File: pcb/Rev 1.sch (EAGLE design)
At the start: 216 parts, among them J1 3220-10-0100-00, J2 10118194-0001LF, J3 B2B-PH-K-S(LF)(SN), Q1 MMBT3904,215MMBT3904,215, Q12 MMBT3904,215MMBT3904,215, Q13 MMBT3904,215MMBT3904,215, Q14 MMBT3904,215MMBT3904,215, Q15 MMBT3904,215MMBT3904,215, Q16 TEFT4300, Q17 TEFT4300, Q18 TEFT4300, Q19 TEFT4300, Q20 MMBT3904,215MMBT3904,215, Q21 MMBT3904,215MMBT3904,215, Q22 MMBT3904,215MMBT3904,215, Q23 MMBT3904,215MMBT3904,215, Q24 TEFT4300, Q25 TEFT4300, Q26 TEFT4300, Q27 TEFT4300, Q28 SI7157DP, Q29 SI7157DP, Q30 MMBT3906, Q31 MMBT3906, Q32 SI7157DP, Q33 MMBT3906, Q34 MMBT3906, U1 ATSAMD21G18A-MU, U10 DRV8871, U11 PCAL6416A, U12 MAX7315, U2 AP3441, U3 TPS61089, U4 BNO055, U5 MCP73811, U7 DRV8871, U8 DRV8871, U9 DRV8871

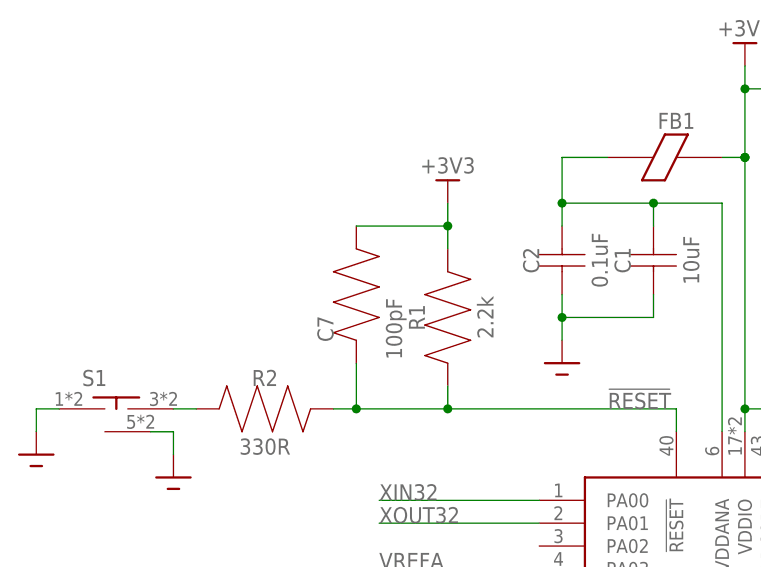
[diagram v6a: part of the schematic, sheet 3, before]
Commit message: Fixed C7 that was somehow a resistor
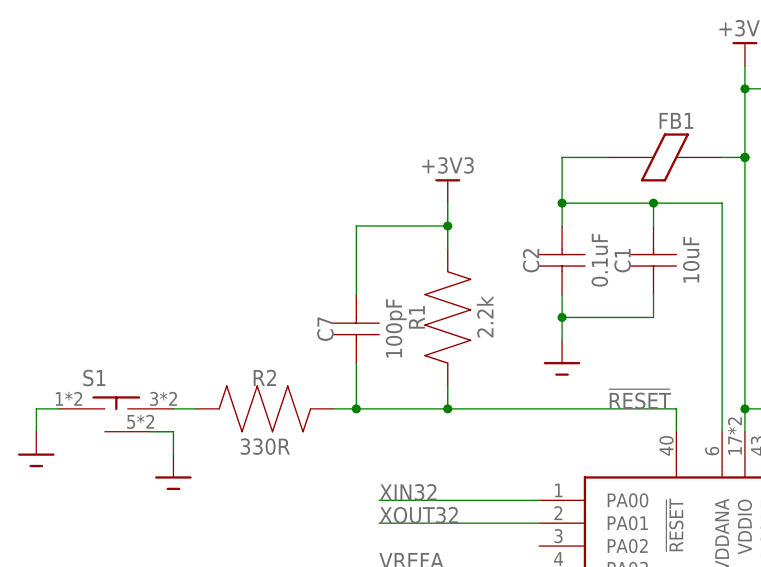
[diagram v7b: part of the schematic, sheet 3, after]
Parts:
- C7: device Micromouse 2020:RESISTOR0603 -> Micromouse 2020:CAPACITOR0603
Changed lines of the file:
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@@
 <part name="GND4" library="Micromouse 2020" deviceset="GND" device=""/>
 <part name="GND3" library="Micromouse 2020" deviceset="GND" device=""/>
-<part name="C7" library="Micromouse 2020" deviceset="RESISTOR" device="0603" package3d_urn="urn:adsk.eagle:package:16053670/1" value="100pF"/>
+<part name="C7" library="Micromouse 2020" deviceset="CAPACITOR" device="0603" package3d_urn="urn:adsk.eagle:package:16053670/1" value="100pF"/>
 <part name="R2" library="Micromouse 2020" deviceset="RESISTOR" device="0805" value="330R"/>
 <part name="S1" library="Micromouse 2020" deviceset="PTS526SMG15SMTR2LFS" device=""/>
@@
 <pinref part="C7" gate="G$1" pin="P$2"/>
 <wire x1="-33.02" y1="68.58" x2="-33.02" y2="71.12" width="0.1524" layer="91"/>
+<wire x1="-43.18" y1="60.96" x2="-43.18" y2="68.58" width="0.1524" layer="91"/>
 <wire x1="-43.18" y1="68.58" x2="-33.02" y2="68.58" width="0.1524" layer="91"/>
 <junction x="-33.02" y="68.58"/>

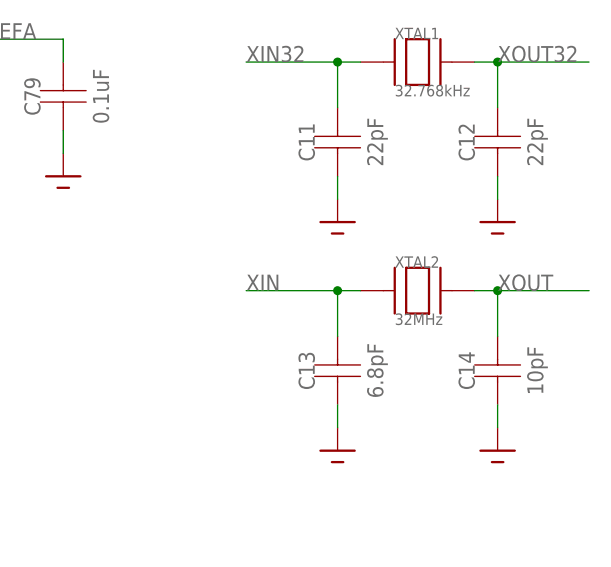
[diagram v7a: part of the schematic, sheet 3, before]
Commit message: Fixed crystal package
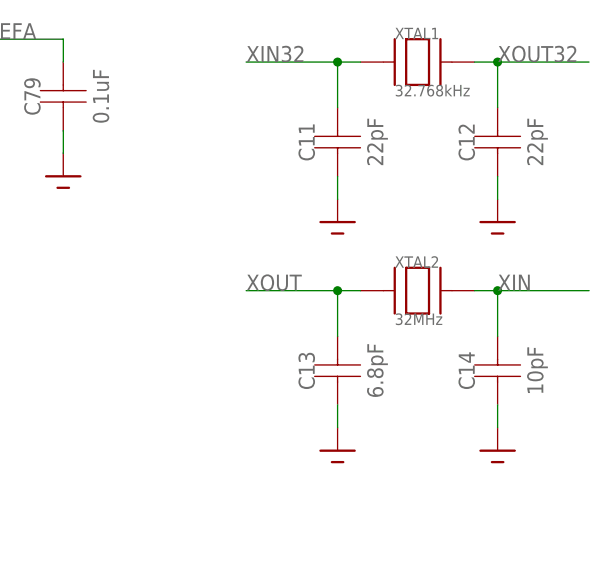
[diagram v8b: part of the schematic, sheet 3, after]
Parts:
- R40: device Micromouse 2020:RESISTOR0805 -> Micromouse 2020:RESISTOR0603
- XTAL2: device Micromouse 2020:FC-135 -> Micromouse 2020:XRCGB
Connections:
- net XIN: now also C14.P$2, XTAL2.P$2; no longer C13.P$2, XTAL2.P$1
- net XOUT: now also C13.P$2, XTAL2.P$1; no longer C14.P$2, XTAL2.P$2
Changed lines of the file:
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@@
 <part name="GND9" library="Micromouse 2020" deviceset="GND" device=""/>
 <part name="GND10" library="Micromouse 2020" deviceset="GND" device=""/>
-<part name="XTAL2" library="Micromouse 2020" deviceset="FC-135" device="" package3d_urn="urn:adsk.eagle:package:14566881/1" value="32MHz"/>
+<part name="XTAL2" library="Micromouse 2020" deviceset="XRCGB" device="" package3d_urn="urn:adsk.eagle:package:14566896/1" value="32MHz"/>
 <part name="C13" library="Micromouse 2020" deviceset="CAPACITOR" device="0402" package3d_urn="urn:adsk.eagle:package:16053683/1" value="6.8pF"/>
 <part name="C14" library="Micromouse 2020" deviceset="CAPACITOR" device="0402" package3d_urn="urn:adsk.eagle:package:16053683/1" value="10pF"/>
@@
 <part name="Q26" library="Micromouse 2020" deviceset="TEFT4300" device="" package3d_urn="urn:adsk.eagle:package:14528166/1"/>
 <part name="P+37" library="Micromouse 2020" deviceset="+3V3" device=""/>
-<part name="R40" library="Micromouse 2020" deviceset="RESISTOR" device="0805" value="1k"/>
+<part name="R40" library="Micromouse 2020" deviceset="RESISTOR" device="0603" package3d_urn="urn:adsk.eagle:package:16053670/1" value="1k"/>
 <part name="GND47" library="Micromouse 2020" deviceset="GND" device=""/>
 <part name="Q27" library="Micromouse 2020" deviceset="TEFT4300" device="" package3d_urn="urn:adsk.eagle:package:14528166/1"/>
@@
 </segment>
 <segment>
+<pinref part="XTAL2" gate="G$1" pin="P$2"/>
+<wire x1="185.42" y1="30.48" x2="187.96" y2="30.48" width="0.1524" layer="91"/>
+<pinref part="C14" gate="G$1" pin="P$2"/>
+<wire x1="187.96" y1="30.48" x2="198.12" y2="30.48" width="0.1524" layer="91"/>
+<wire x1="187.96" y1="30.48" x2="187.96" y2="25.4" width="0.1524" layer="91"/>
+<junction x="187.96" y="30.48"/>
+<label x="187.96" y="30.48" size="1.778" layer="95"/>
+</segment>
+</net>
+<net name="XOUT" class="0">
+<segment>
+<pinref part="U1" gate="G$1" pin="PA15"/>
+<wire x1="-40.64" y1="0" x2="-22.86" y2="0" width="0.1524" layer="91"/>
+<label x="-40.64" y="0" size="1.778" layer="95"/>
+</segment>
+<segment>
 <pinref part="C13" gate="G$1" pin="P$2"/>
 <wire x1="170.18" y1="25.4" x2="170.18" y2="30.48" width="0.1524" layer="91"/>
@@
 </segment>
 </net>
-<net name="XOUT" class="0">
-<segment>
-<pinref part="U1" gate="G$1" pin="PA15"/>
-<wire x1="-40.64" y1="0" x2="-22.86" y2="0" width="0.1524" layer="91"/>
-<label x="-40.64" y="0" size="1.778" layer="95"/>
-</segment>
-<segment>
-<pinref part="XTAL2" gate="G$1" pin="P$2"/>
-<wire x1="185.42" y1="30.48" x2="187.96" y2="30.48" width="0.1524" layer="91"/>
-<pinref part="C14" gate="G$1" pin="P$2"/>
-<wire x1="187.96" y1="30.48" x2="198.12" y2="30.48" width="0.1524" layer="91"/>
-<wire x1="187.96" y1="30.48" x2="187.96" y2="25.4" width="0.1524" layer="91"/>
-<junction x="187.96" y="30.48"/>
-<label x="187.96" y="30.48" size="1.778" layer="95"/>
-</segment>
-</net>
